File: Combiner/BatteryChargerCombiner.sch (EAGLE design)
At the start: 183 parts, among them Q1 DMN6040SSD-13, Q10 4.3A/20V/54mΩ, Q11 4.3A/20V/54mΩ, Q2 DMN6040SSD-13, Q3 DMN6040SSD-13, Q4 DMN6040SSD-13, Q5 DMP4047SSD-13, Q6 220mA/50V/3.5Ω, Q7 220mA/50V/3.5Ω, Q8 4.3A/20V/54mΩ, Q9 4.3A/20V/54mΩ, U1 BQ24650, U10 TS7211, U11 MIC5219 3.3V, U12 MKR1000-SMD, U13 STWD100, U14 74AUC1G06DBV, U15 74AUC1G06DBV, U16 74AUC1G06DBV, U17 LMV358, U2 BQ28Z610, U3 BQ28Z610, U4 BQ24650, U5 TCA9543A, U6 WE-78, U7 WE-78, U8 74AHC1G07DBV, U9 74AUC1G06DBV

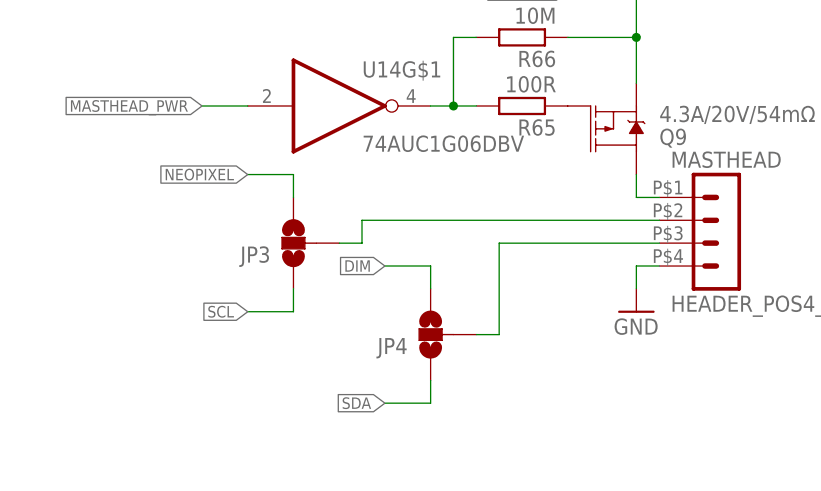
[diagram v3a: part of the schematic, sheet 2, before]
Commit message: Shrunk board width to 1600 mil, so it will fit inside a 1.5 in PVC pipe
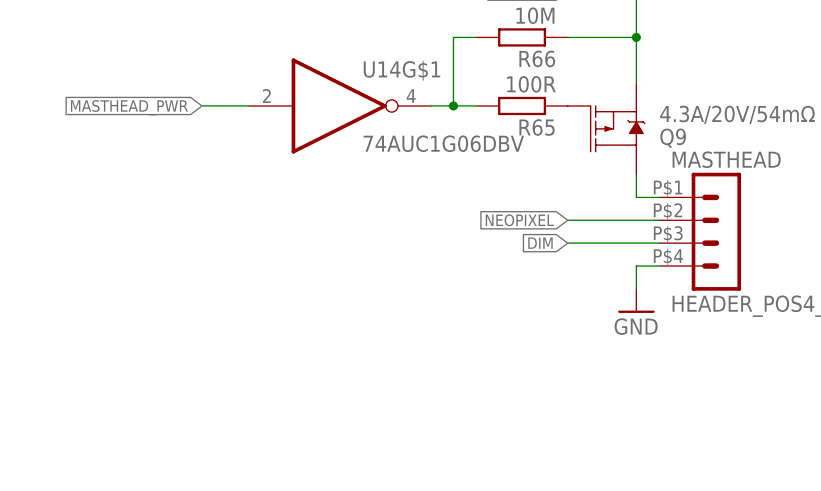
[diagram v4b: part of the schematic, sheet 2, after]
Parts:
- removed JP3, JP4: JUMPER-SMT_3_NO_SILK, SparkFun-Jumpers:JUMPER-SMT_3_NO_SILK
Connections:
- removed net N$14: JP3.2, MASTHEAD.2
- removed net N$47: JP4.2, MASTHEAD.3
- net DIM: now also MASTHEAD.3; no longer JP4.3
- net NEOPIXEL: now also MASTHEAD.2; no longer JP3.3
- net SCL: no longer JP3.1
- net SDA: no longer JP4.1
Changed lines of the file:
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@@
 <part name="+3V10" library="supply1" library_urn="urn:adsk.eagle:library:371" deviceset="+3V3" device=""/>
 <part name="GND44" library="supply1" library_urn="urn:adsk.eagle:library:371" deviceset="GND" device=""/>
-<part name="JP3" library="SparkFun-Jumpers" library_urn="urn:adsk.eagle:library:528" deviceset="JUMPER-SMT_3_NO" device="_SILK" package3d_urn="urn:adsk.eagle:package:39285/1"/>
-<part name="JP4" library="SparkFun-Jumpers" library_urn="urn:adsk.eagle:library:528" deviceset="JUMPER-SMT_3_NO" device="_SILK" package3d_urn="urn:adsk.eagle:package:39285/1"/>
 </parts>
 <sheets>
@@
 <instance part="+3V10" gate="G$1" x="248.92" y="71.12"/>
 <instance part="GND44" gate="1" x="248.92" y="40.64"/>
-<instance part="JP3" gate="G$1" x="35.56" y="25.4" smashed="yes" rot="R180">
-<attribute name="NAME" x="33.02" y="25.019" size="1.778" layer="95" font="vector" rot="R180"/>
-</instance>
-<instance part="JP4" gate="G$1" x="50.8" y="15.24" smashed="yes" rot="R180">
-<attribute name="NAME" x="48.26" y="14.859" size="1.778" layer="95" font="vector" rot="R180"/>
-</instance>
 </instances>
 <busses>
@@
 <label x="241.3" y="101.6" size="1.27" layer="95" rot="R180" xref="yes"/>
 </segment>
-<segment>
-<pinref part="JP4" gate="G$1" pin="1"/>
-<wire x1="50.8" y1="10.16" x2="50.8" y2="7.62" width="0.1524" layer="91"/>
-<wire x1="50.8" y1="7.62" x2="45.72" y2="7.62" width="0.1524" layer="91"/>
-<label x="45.72" y="7.62" size="1.27" layer="95" rot="R180" xref="yes"/>
-</segment>
 </net>
 <net name="SCL" class="0">
@@
 <wire x1="241.3" y1="99.06" x2="246.38" y2="99.06" width="0.1524" layer="91"/>
 <label x="241.3" y="99.06" size="1.27" layer="95" rot="R180" xref="yes"/>
-</segment>
-<segment>
-<pinref part="JP3" gate="G$1" pin="1"/>
-<wire x1="35.56" y1="20.32" x2="35.56" y2="17.78" width="0.1524" layer="91"/>
-<wire x1="35.56" y1="17.78" x2="30.48" y2="17.78" width="0.1524" layer="91"/>
-<label x="30.48" y="17.78" size="1.27" layer="95" rot="R180" xref="yes"/>
 </segment>
 </net>
@@
 </segment>
 <segment>
-<pinref part="JP3" gate="G$1" pin="3"/>
-<wire x1="35.56" y1="30.48" x2="35.56" y2="33.02" width="0.1524" layer="91"/>
-<wire x1="35.56" y1="33.02" x2="30.48" y2="33.02" width="0.1524" layer="91"/>
-<label x="30.48" y="33.02" size="1.27" layer="95" rot="R180" xref="yes"/>
+<label x="66.04" y="27.94" size="1.27" layer="95" rot="R180" xref="yes"/>
+<pinref part="MASTHEAD" gate="G$1" pin="2"/>
+<wire x1="66.04" y1="27.94" x2="76.2" y2="27.94" width="0.1524" layer="91"/>
 </segment>
 </net>
@@
 </segment>
 <segment>
-<pinref part="JP4" gate="G$1" pin="3"/>
-<wire x1="50.8" y1="20.32" x2="50.8" y2="22.86" width="0.1524" layer="91"/>
-<wire x1="50.8" y1="22.86" x2="45.72" y2="22.86" width="0.1524" layer="91"/>
-<label x="45.72" y="22.86" size="1.27" layer="95" rot="R180" xref="yes"/>
+<label x="66.04" y="25.4" size="1.27" layer="95" rot="R180" xref="yes"/>
+<pinref part="MASTHEAD" gate="G$1" pin="3"/>
+<wire x1="66.04" y1="25.4" x2="76.2" y2="25.4" width="0.1524" layer="91"/>
 </segment>
 </net>
@@
 </segment>
 </net>
-<net name="N$14" class="0">
-<segment>
-<pinref part="MASTHEAD" gate="G$1" pin="2"/>
-<pinref part="JP3" gate="G$1" pin="2"/>
-<wire x1="40.64" y1="25.4" x2="43.18" y2="25.4" width="0.1524" layer="91"/>
-<wire x1="43.18" y1="25.4" x2="43.18" y2="27.94" width="0.1524" layer="91"/>
-<wire x1="43.18" y1="27.94" x2="76.2" y2="27.94" width="0.1524" layer="91"/>
-</segment>
-</net>
-<net name="N$47" class="0">
-<segment>
-<pinref part="MASTHEAD" gate="G$1" pin="3"/>
-<pinref part="JP4" gate="G$1" pin="2"/>
-<wire x1="55.88" y1="15.24" x2="58.42" y2="15.24" width="0.1524" layer="91"/>
-<wire x1="58.42" y1="15.24" x2="58.42" y2="25.4" width="0.1524" layer="91"/>
-<wire x1="58.42" y1="25.4" x2="76.2" y2="25.4" width="0.1524" layer="91"/>
-</segment>
-</net>

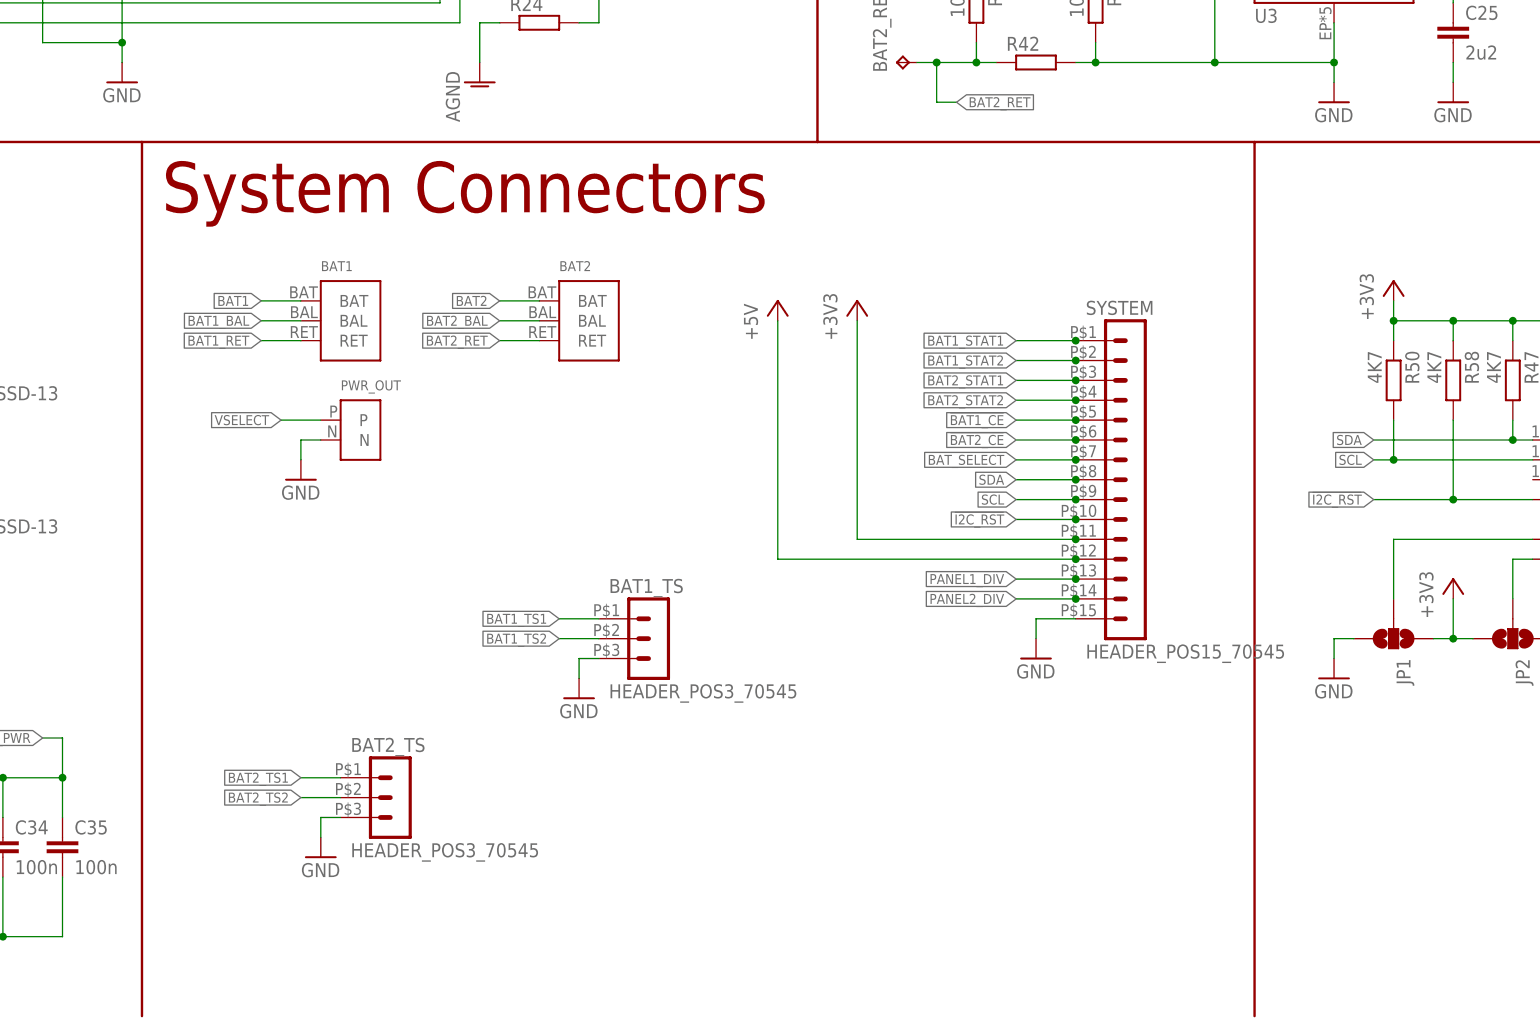
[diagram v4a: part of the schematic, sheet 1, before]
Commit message: Now with idiot lights; still need to fix silkscreen around lights
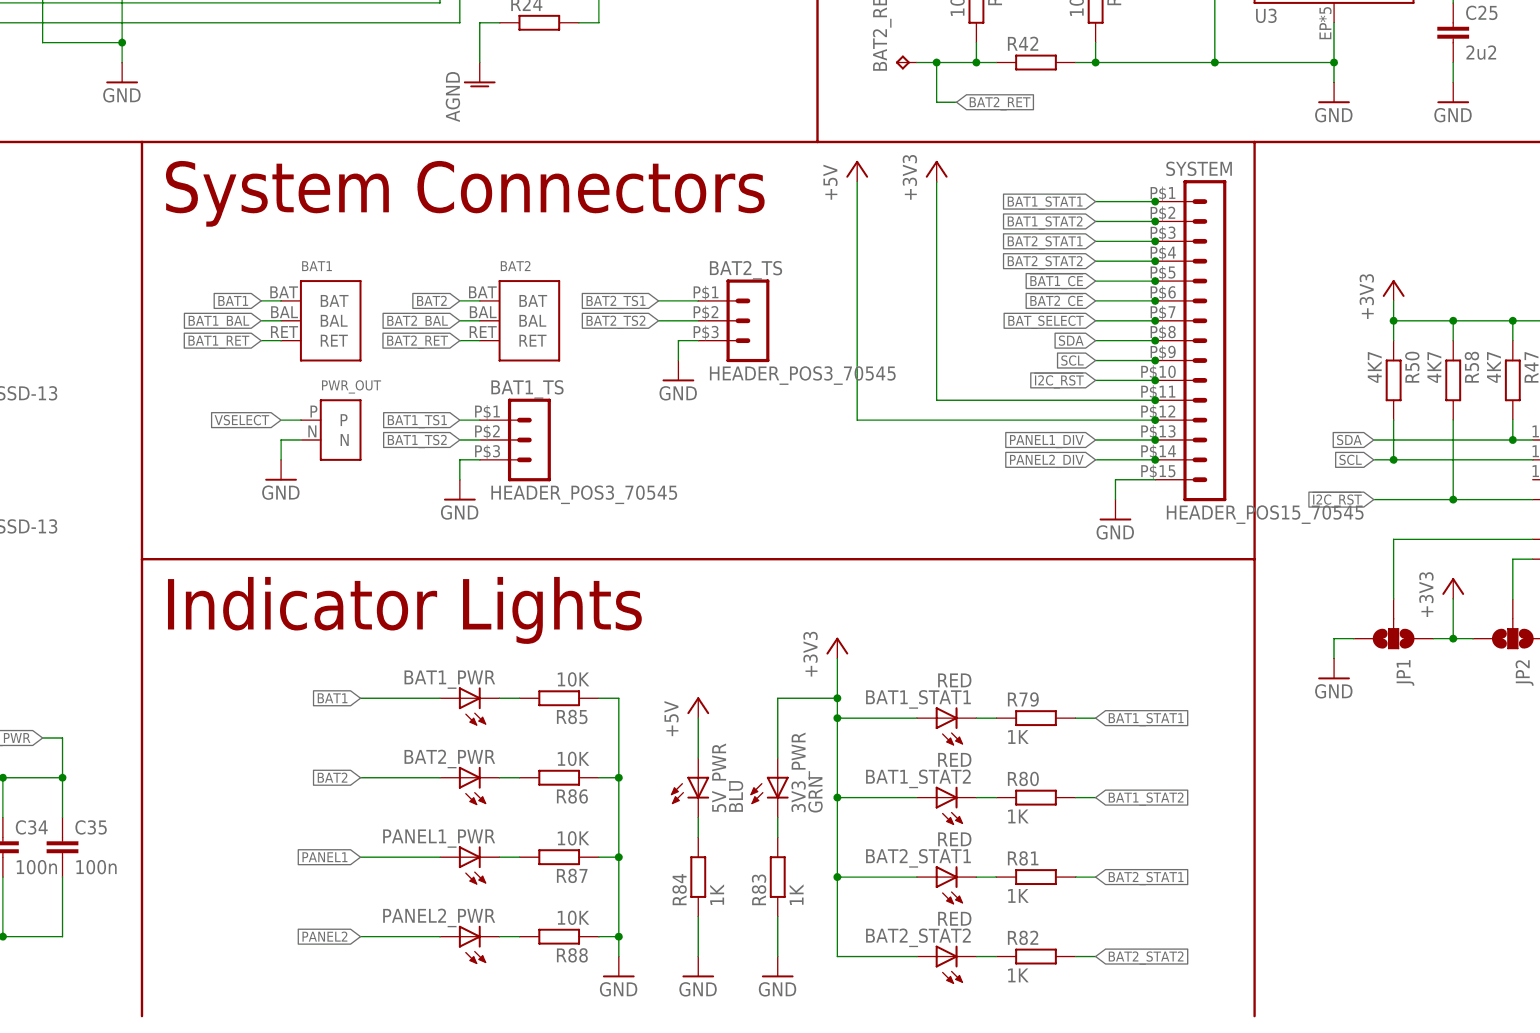
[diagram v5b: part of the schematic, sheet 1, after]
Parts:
- added 3V3_PWR: GRN, adafruit:LEDCHIP-LED0603
- added 5V_PWR: BLU, adafruit:LEDCHIP-LED0603
- added BAT1_PWR, BAT2_PWR, PANEL1_PWR, PANEL2_PWR: (no value), adafruit:LEDCHIP-LED0603
- added BAT1_STAT1, BAT1_STAT2, BAT2_STAT1, BAT2_STAT2: RED, adafruit:LEDCHIP-LED0603
- added R79, R80, R81, R82, R83, R84: 1K, resistor:R-EU_R0603
- added R85, R86, R87, R88: 10K, resistor:R-EU_R0603
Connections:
- new net N$14: BAT1_STAT1.C, R79.1
- new net N$47: BAT1_STAT2.C, R80.1
- new net N$49: BAT2_STAT1.C, R81.1
- new net N$56: BAT2_STAT2.C, R82.1
- new net N$74: 3V3_PWR.C, R83.2
- new net N$77: 5V_PWR.C, R84.2
- new net N$81: BAT1_PWR.C, R85.2
- new net N$82: BAT2_PWR.C, R86.2
- new net N$83: PANEL1_PWR.C, R87.2
- new net N$84: PANEL2_PWR.C, R88.2
- net +3V3: now also 3V3_PWR.A, BAT1_STAT1.A, BAT1_STAT2.A, BAT2_STAT1.A, BAT2_STAT2.A
- net +5V: now also 5V_PWR.A
- net BAT1: now also BAT1_PWR.A
- net BAT1_STAT1: now also R79.2
- net BAT1_STAT2: now also R80.2
- net BAT2: now also BAT2_PWR.A
- net BAT2_STAT1: now also R81.2
- net BAT2_STAT2: now also R82.2
- net GND: now also R83.1, R84.1, R85.1, R86.1, R87.1, R88.1
- net PANEL1: now also PANEL1_PWR.A
- net PANEL2: now also PANEL2_PWR.A
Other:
- note added: "Indicator Lights"
- moved on the sheet: BAT1, BAT1_TS, BAT2, BAT2_TS, PWR_OUT, SYSTEM

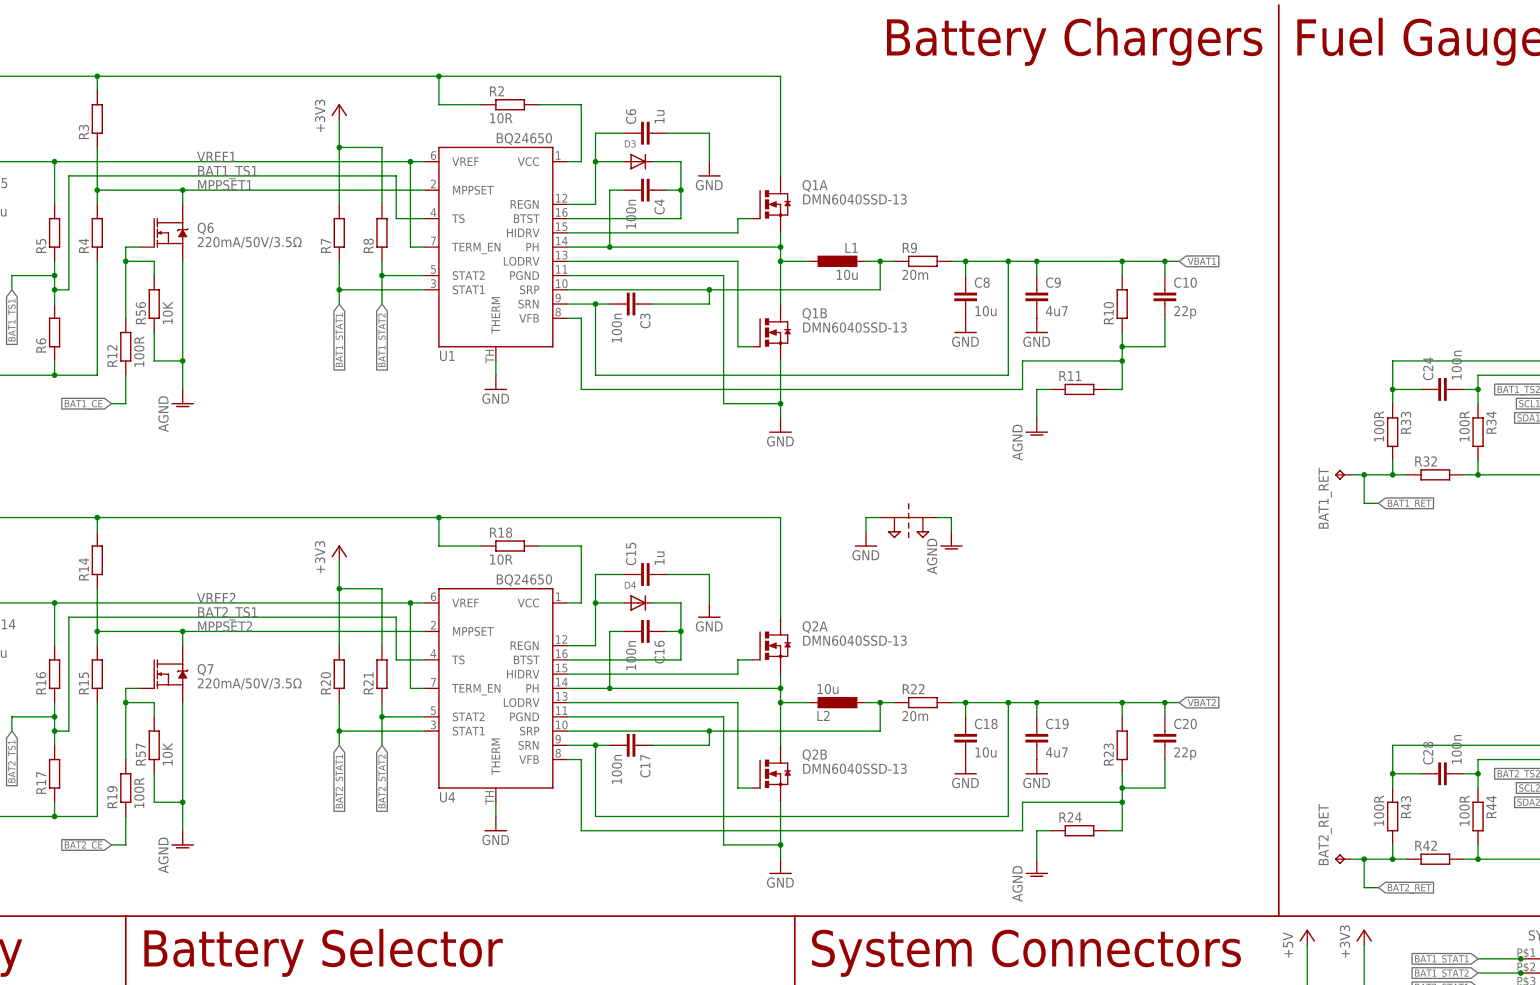
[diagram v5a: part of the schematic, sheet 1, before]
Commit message: Put together BoM for battery charger/combiner. Left out everything except the trim resistors for the temp sensor'
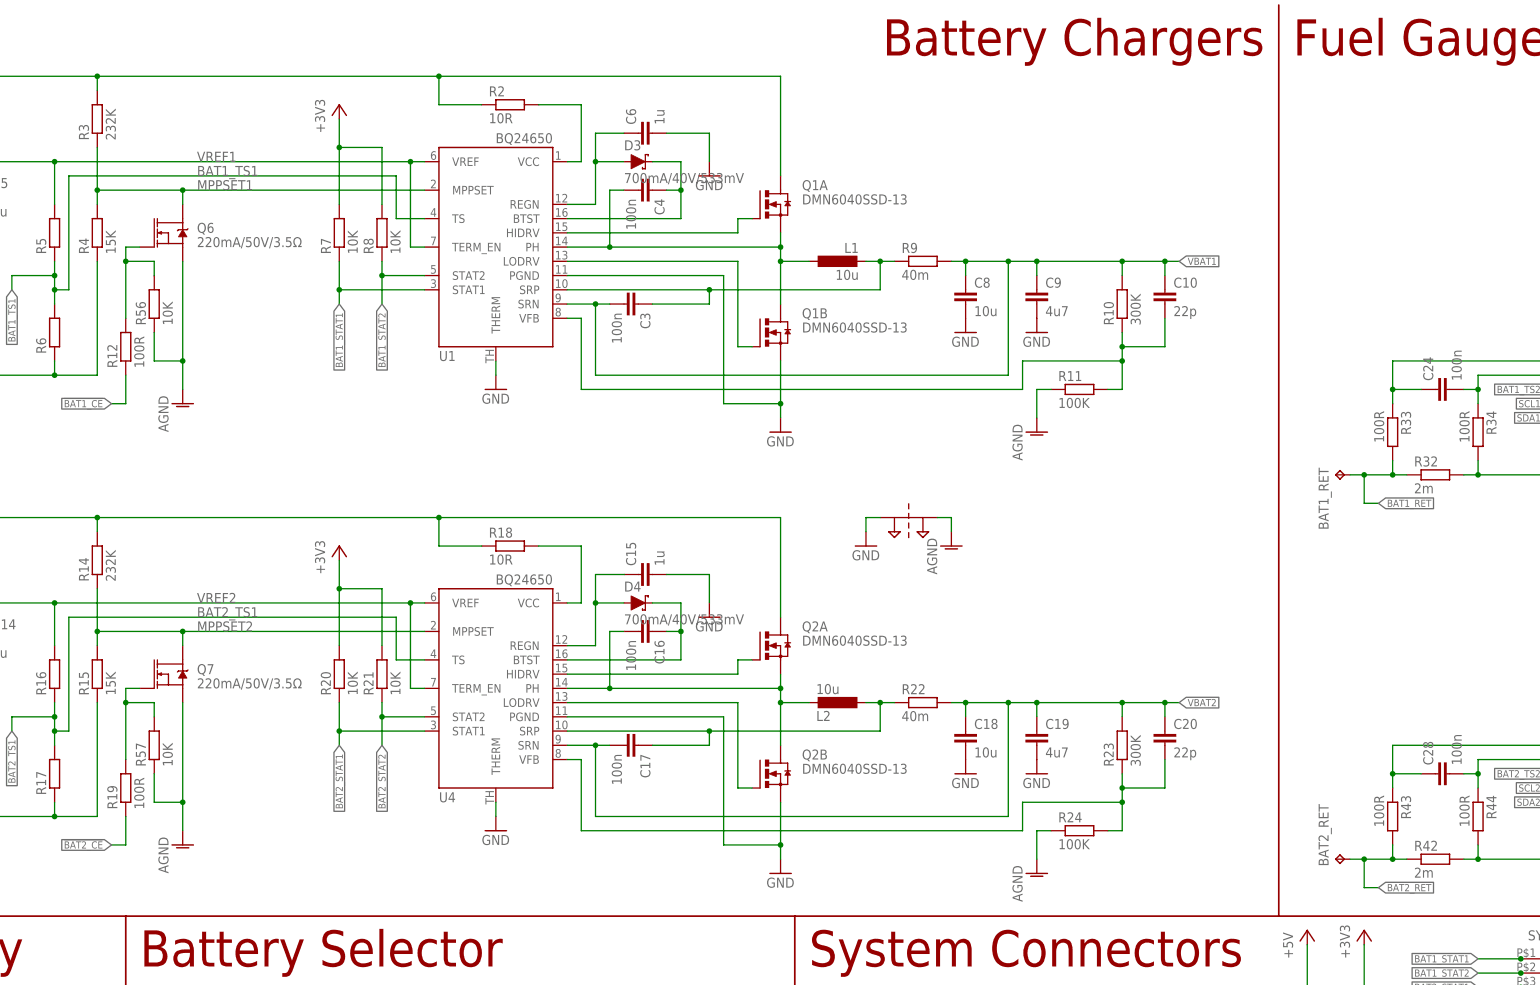
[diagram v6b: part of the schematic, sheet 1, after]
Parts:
- C1, C11: device resistor:C-EUC0805 -> resistor:C-EUC0603
- D3, D4: value (none) -> 700mA/40V/533mV; device adafruit:DIODESOT23_REFLOW -> SparkFun-DiscreteSemi:DIODE-SCHOTTKY-ZLLS500
- R10, R23: value (none) -> 300K
- R11, R24: value (none) -> 100K
- R14, R3: value (none) -> 232K
- R15, R4, R59, R74, R76: value (none) -> 15K
- R20, R21, R60, R7, R73, R75, R77, R78, R8: value (none) -> 10K
- R22, R9: value 20m -> 40m
- R32, R42: value (none) -> 2m
- R61, R63: value (none) -> 75K
- R62, R64: value (none) -> 12K
